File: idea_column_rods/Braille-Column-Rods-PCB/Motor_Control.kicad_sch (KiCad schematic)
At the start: 7 parts, among them U14 74HC595, U15 74HC595, U30 CD74HC4067M

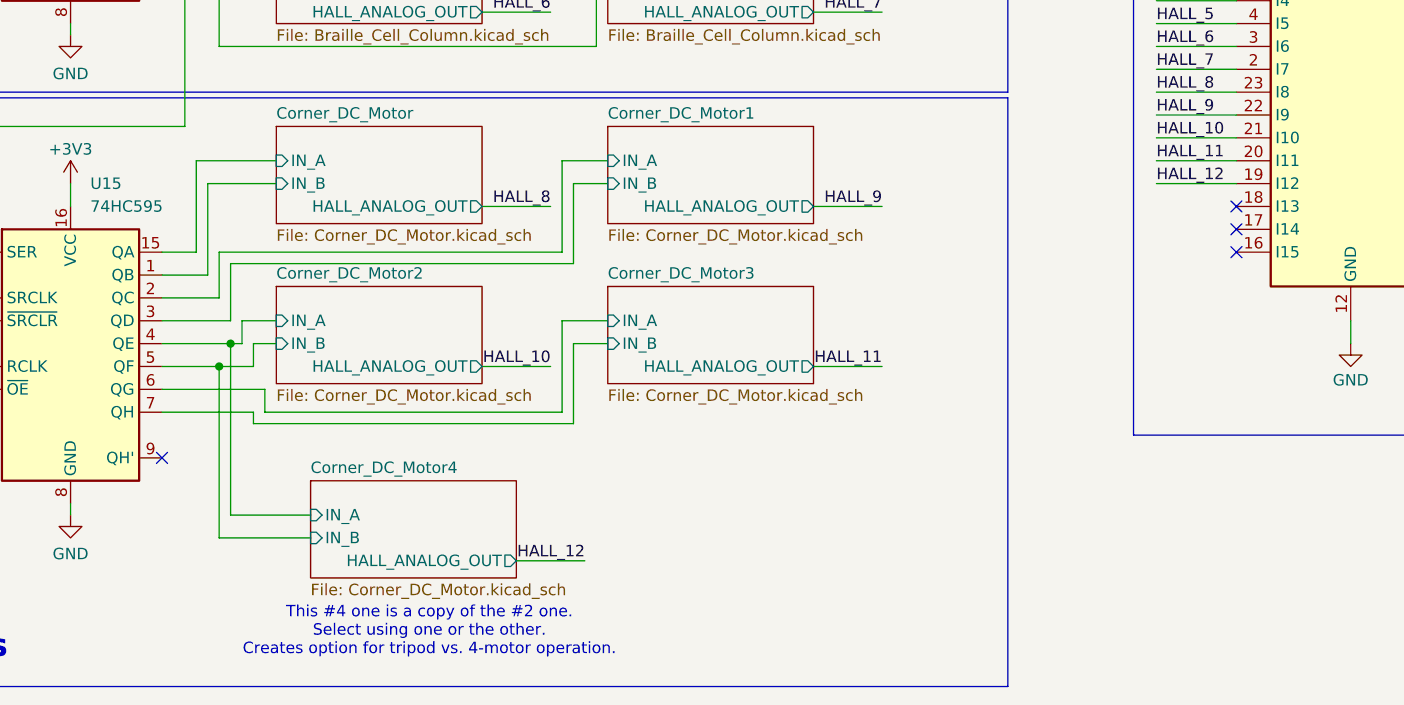
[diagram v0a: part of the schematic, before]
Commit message: Create PCB and CAD for Type 4 Rev 1 rod cams (#13)
* WIP: Rods PCB placement

* WIP: Place the housing and motor X

* WIP: Position everything

* WIP: Update tight placement of DC motor

* WIP: Layout and route the stepper driver

* WIP: Motor layout is good

* WIP: Manual routing and silkscreens

* Comments

* Big routing

* Clean up DRC (mostly footprints)

* Fix spacing issue on top

* Fix spacing issues on bottom

* Create render of 6mm motor, add to PCB

* WIP: Get cams good

* WIP: Reorder the cam bushing and hall sensor

* Finish and tag release

* Complete type 4 rev 1

* Create dc_motor_clamp cad
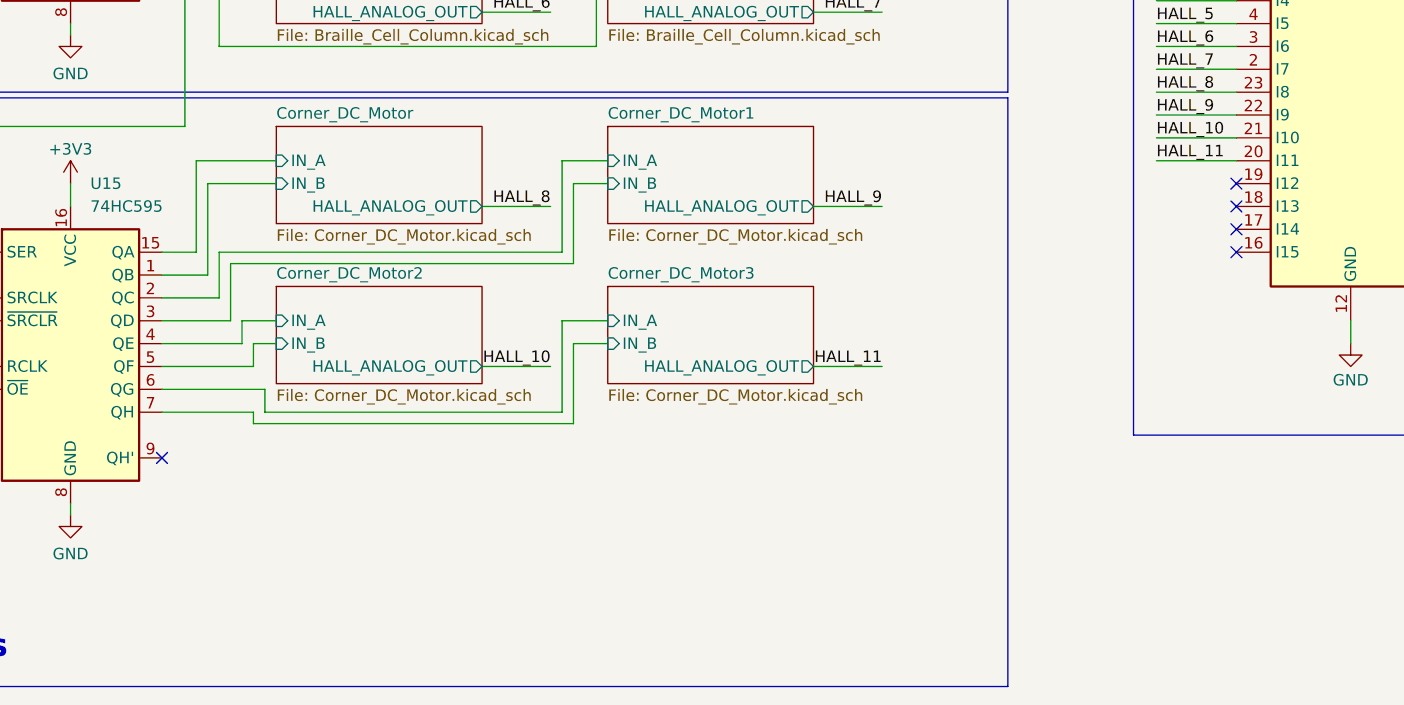
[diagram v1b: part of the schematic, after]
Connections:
- net HALL_12: no longer names the net of U30.19 (I12)
- no-connect marks 12 -> 13
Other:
- removed sheet Corner_DC_Motor4
- note removed: "This #4 one is a copy of the #2 one. Select using one or the other. Creates option for tripod vs. 4-motor operation."
- title: (none) -> Braille Cam Rod Prototype (Type 4)
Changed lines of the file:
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@@
 	(generator_version "8.0")
 	(paper "USLetter")
-	(junction
-		(at 80.01 121.92)
-		(diameter 0)
-		(color 0 0 0 0)
-	)
-	(junction
-		(at 78.74 124.46)
-		(diameter 0)
-		(color 0 0 0 0)
+	(title_block
+		(title "Braille Cam Rod Prototype (Type 4)")
+		(date "2025-01-06")
+		(rev "Rev 1")
 	)
 	(no_connect
@@
 	)
 	(no_connect
+		(at 191.77 104.14)
+	)
+	(no_connect
 		(at 85.09 60.96)
 	)
@@
 	(wire
 		(pts
-			(xy 111.76 146.05) (xy 119.38 146.05)
-		)
-		(stroke
-			(width 0)
-			(type default)
-		)
-	)
-	(wire
-		(pts
 			(xy 144.78 85.09) (xy 152.4 85.09)
 		)
@@
 	(wire
 		(pts
-			(xy 88.9 143.51) (xy 78.74 143.51)
-		)
-		(stroke
-			(width 0)
-			(type default)
-		)
-	)
-	(wire
-		(pts
 			(xy 72.39 66.04) (xy 81.28 66.04)
 		)
@@
 	(wire
 		(pts
-			(xy 182.88 104.14) (xy 191.77 104.14)
-		)
-		(stroke
-			(width 0)
-			(type default)
-		)
-	)
-	(wire
-		(pts
 			(xy 77.47 104.14) (xy 85.09 104.14)
 		)
@@
 	(wire
 		(pts
-			(xy 78.74 143.51) (xy 78.74 124.46)
-		)
-		(stroke
-			(width 0)
-			(type default)
-		)
-	)
-	(wire
-		(pts
 			(xy 116.84 129.54) (xy 116.84 119.38)
 		)
@@
 	(wire
 		(pts
-			(xy 78.74 124.46) (xy 82.55 124.46)
+			(xy 72.39 124.46) (xy 82.55 124.46)
 		)
 		(stroke
@@
 	(wire
 		(pts
-			(xy 72.39 121.92) (xy 80.01 121.92)
+			(xy 72.39 121.92) (xy 81.28 121.92)
 		)
 		(stroke
@@
 	(wire
 		(pts
-			(xy 72.39 124.46) (xy 78.74 124.46)
-		)
-		(stroke
-			(width 0)
-			(type default)
-		)
-	)
-	(wire
-		(pts
 			(xy 80.01 113.03) (xy 118.11 113.03)
 		)
@@
 	(wire
 		(pts
-			(xy 88.9 140.97) (xy 80.01 140.97)
-		)
-		(stroke
-			(width 0)
-			(type default)
-		)
-	)
-	(wire
-		(pts
 			(xy 81.28 119.38) (xy 85.09 119.38)
 		)
@@
 	(wire
 		(pts
-			(xy 80.01 121.92) (xy 81.28 121.92)
-		)
-		(stroke
-			(width 0)
-			(type default)
-		)
-	)
-	(wire
-		(pts
 			(xy 62.23 87.63) (xy 62.23 86.36)
 		)
@@
 	(wire
 		(pts
-			(xy 80.01 140.97) (xy 80.01 121.92)
-		)
-		(stroke
-			(width 0)
-			(type default)
-		)
-	)
-	(wire
-		(pts
 			(xy 48.26 66.04) (xy 52.07 66.04)
 		)
@@
 		)
 	)
-	(text "This #4 one is a copy of the #2 one.\nSelect using one or the other.\nCreates option for tripod vs. 4-motor operation."
-		(exclude_from_sim no)
-		(at 102.108 153.924 0)
-		(effects
-			(font
-				(size 1.27 1.27)
-			)
-		)
-	)
 	(label "HALL_1"
 		(at 182.88 76.2 0)
@@
 		)
 	)
-	(label "HALL_12"
-		(at 119.38 146.05 180)
-		(fields_autoplaced yes)
-		(effects
-			(font
-				(size 1.27 1.27)
-			)
-			(justify right bottom)
-		)
-	)
 	(label "HALL_2"
 		(at 115.57 49.53 180)
@@
 		)
 	)
-	(label "HALL_12"
-		(at 182.88 104.14 0)
-		(fields_autoplaced yes)
-		(effects
-			(font
-				(size 1.27 1.27)
-			)
-			(justify left bottom)
-		)
-	)
 	(label "HALL_11"
 		(at 152.4 124.46 180)
@@
 				)
 			)
-		)
-	)
-	(sheet
-		(at 88.9 137.16)
-		(size 22.86 10.795)
-		(fields_autoplaced yes)
-		(stroke
-			(width 0.1524)
-			(type solid)
-		)
-		(fill
-			(color 0 0 0 0.0000)
-		)
-		(property "Sheetname" "Corner_DC_Motor4"
-			(at 88.9 136.4484 0)
-			(effects
-				(font
-					(size 1.27 1.27)
-				)
-				(justify left bottom)
-			)
-		)
-		(property "Sheetfile" "Corner_DC_Motor.kicad_sch"
-			(at 88.9 148.5396 0)
-			(effects
-				(font
-					(size 1.27 1.27)
-				)
-				(justify left top)
-			)
-		)
-		(pin "IN_A" input
-			(at 88.9 140.97 180)
-			(effects
-				(font
-					(size 1.27 1.27)
-				)
-				(justify left)
-			)
-		)
-		(pin "IN_B" input
-			(at 88.9 143.51 180)
-			(effects
-				(font
-					(size 1.27 1.27)
-				)
-				(justify left)
-			)
-		)
-		(pin "HALL_ANALOG_OUT" output
-			(at 111.76 146.05 0)
-			(effects
-				(font
-					(size 1.27 1.27)
-				)
-				(justify right)
-			)
-		)
-		(instances
-			(project "Braille-Column-Rods-PCB"
-				(path "/f7fdfeea-4cd4-4338-ad68-f9089a17ed6f/1220b182-3f07-4fe8-af47-372abe179b4f"
-					(page "17")
-				)
-			)
